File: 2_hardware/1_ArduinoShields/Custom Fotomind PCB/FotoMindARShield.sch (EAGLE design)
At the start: 11 parts

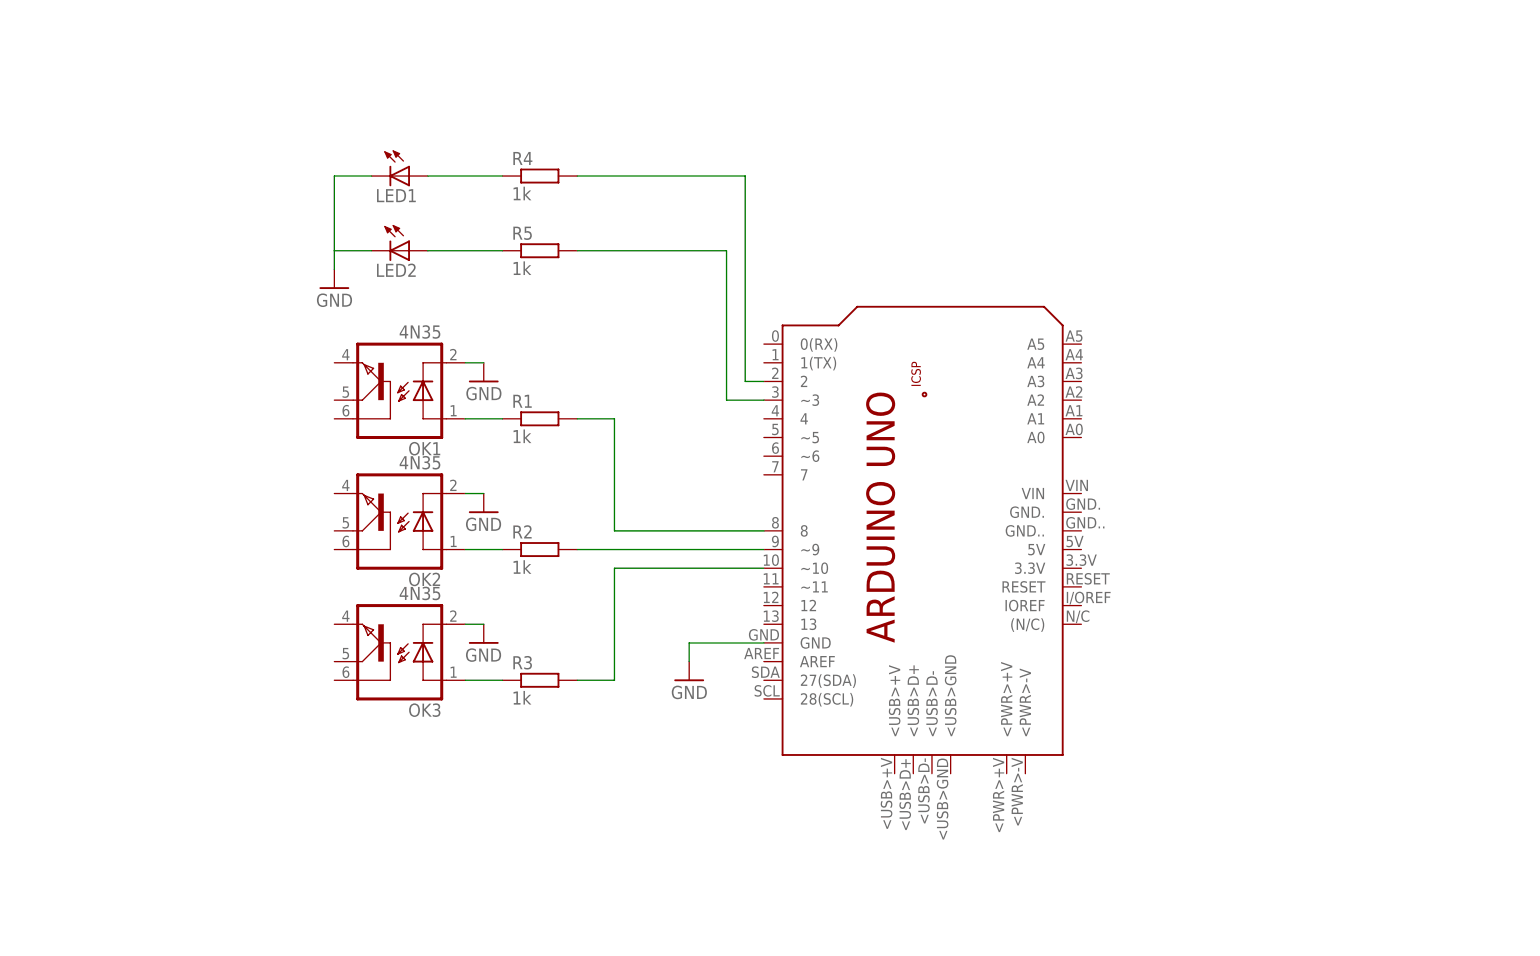
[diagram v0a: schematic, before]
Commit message: PCB: Added FotoResistor & Testbuttons
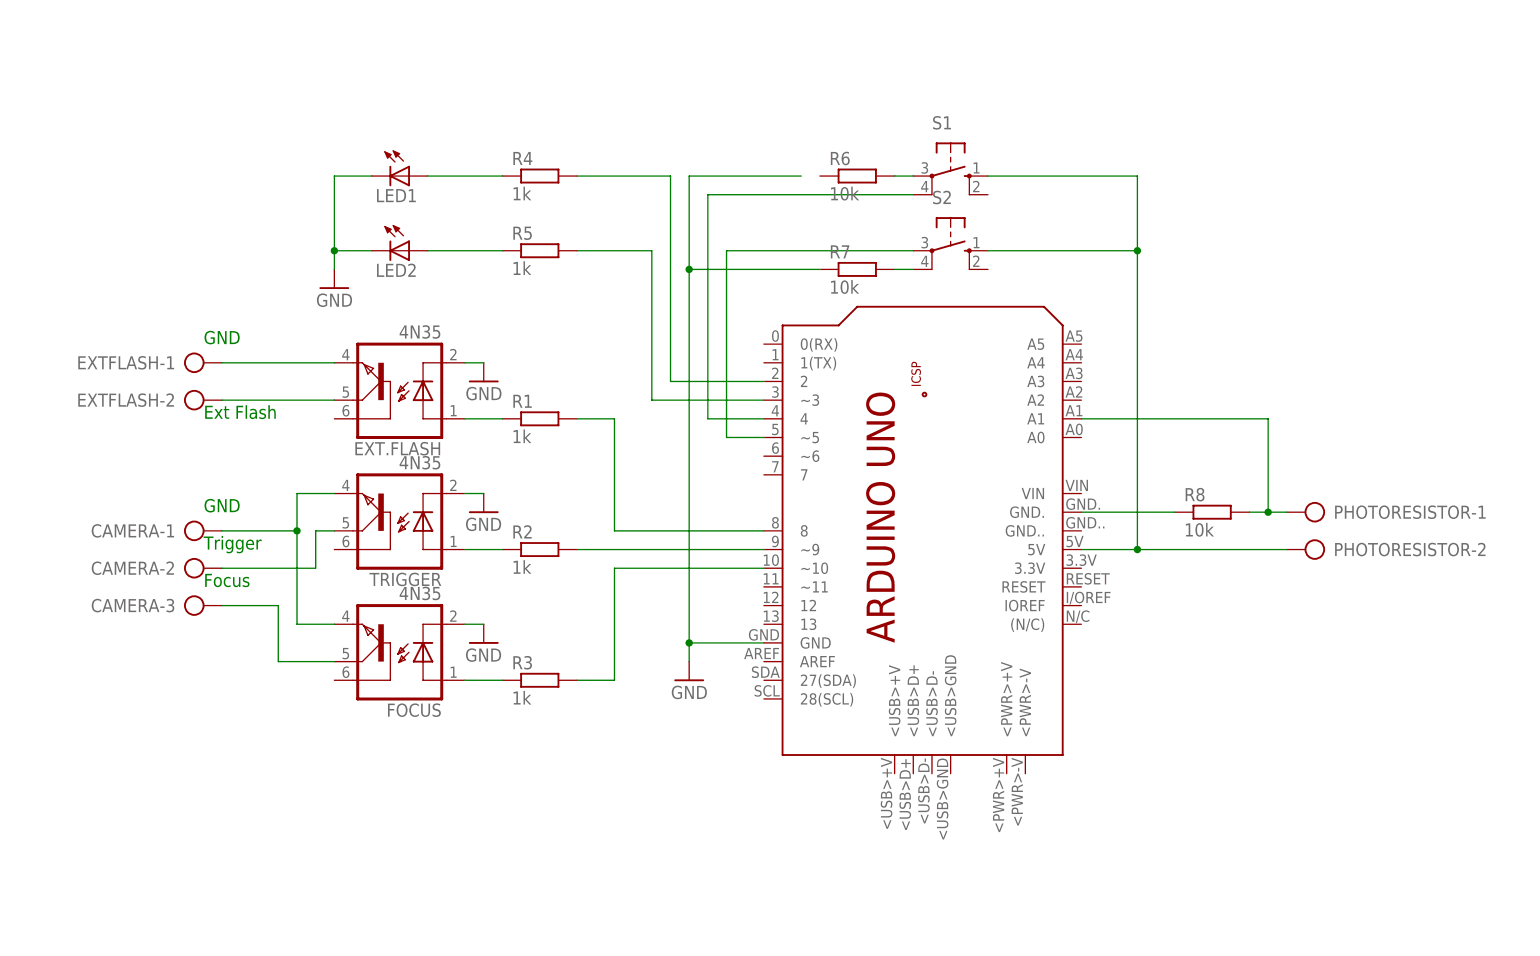
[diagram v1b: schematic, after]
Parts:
- added CAMERA: (no value), con-ptr500:AK300/3
- added EXTFLASH, PHOTORESISTOR: (no value), con-ptr500:AK300/2
- added R6, R7, R8: 10k, eagle-ltspice:R0204/7
- added S1, S2: (no value), switch-omron:10-XX
- renumbered OK1 to EXT.FLASH, OK2 to TRIGGER, OK3 to FOCUS
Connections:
- new net N$11: EXT.FLASH.EMI, EXTFLASH-1.KL
- new net N$12: EXT.FLASH.COL, EXTFLASH-2.KL
- new net N$13: CAMERA-1.KL, FOCUS.EMI, TRIGGER.EMI
- new net N$14: CAMERA-2.KL, TRIGGER.COL
- new net N$15: CAMERA-3.KL, FOCUS.COL
- new net N$16: PCB1.4, S1.P1
- new net N$17: PCB1.~5, S2.P
- new net N$18: R6.2, S1.P
- new net N$19: PCB1.5V, PHOTORESISTOR-2.KL, S1.S, S2.S
- new net N$20: R7.2, S2.P1
- new net N$21: PCB1.GND., R8.1
- new net N$22: PCB1.A1, PHOTORESISTOR-1.KL, R8.2
- net GND: now also R7.1
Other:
- note added: "Ext Flash"
- note added: "Focus"
- note added: "GND"
- note added: "Trigger"

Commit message: Added header for wireless-nRF24-communication
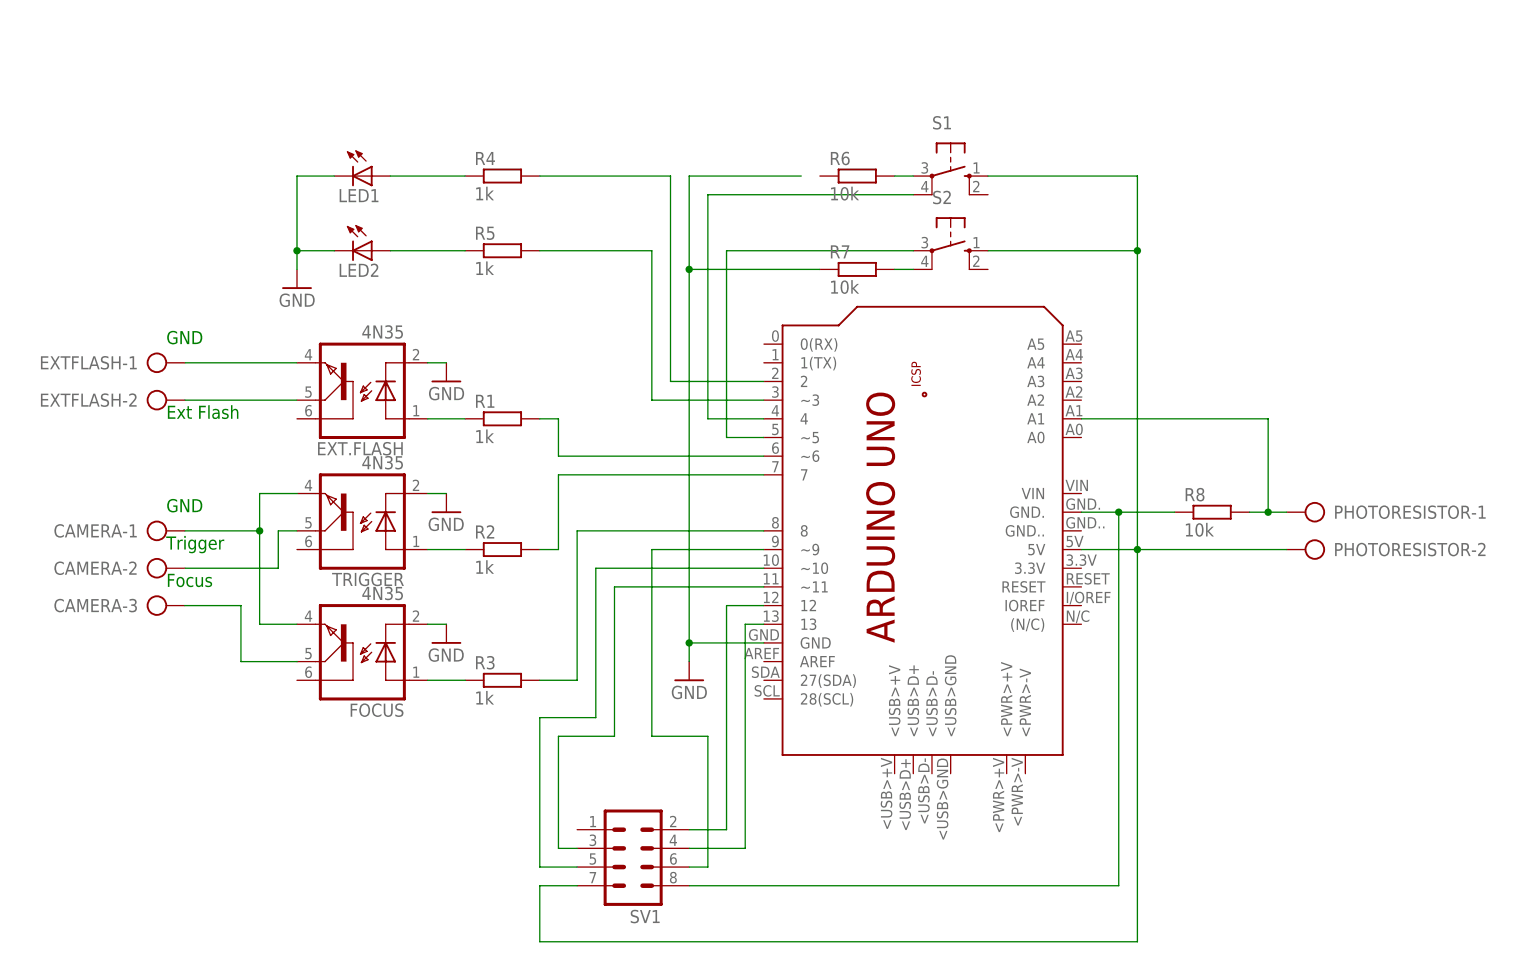
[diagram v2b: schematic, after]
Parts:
- added SV1: (no value), con-lstb:MA04-2
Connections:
- new net N$23: PCB1.12, SV1.2
- new net N$24: PCB1.~11, SV1.3
- new net N$25: PCB1.13, SV1.4
- new net N$26: PCB1.~10, SV1.5
- new net N$27: PCB1.~9, SV1.6
- net N$19: now also SV1.7
- net N$21: now also SV1.8
- net N$4: now also PCB1.~6; no longer PCB1.8
- net N$5: now also PCB1.7; no longer PCB1.~9
- net N$6: now also PCB1.8; no longer PCB1.~10
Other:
- moved on the sheet: CAMERA-1, CAMERA-2, CAMERA-3, EXT.FLASH, EXTFLASH-1, EXTFLASH-2, FOCUS, LED1, LED2, R1, R2, R3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

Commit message: Added Requirements + PCB progress
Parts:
- added EXTPOWER, EXTSENSOR: (no value), con-ptr500:AK300/2
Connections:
- new net N$28: EXTSENSOR-1.KL, PCB1.A0
- new net N$29: EXTSENSOR-2.KL, PCB1.A2
- new net N$30: PCB1.3.3V, SV1.7
- net GND: now also R6.1
- net N$19: now also EXTPOWER-2.KL; no longer SV1.7
- net N$21: now also EXTPOWER-1.KL
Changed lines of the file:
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@@
 <part name="R8" library="eagle-ltspice" deviceset="R" device="0204/7" value="10k"/>
 <part name="SV1" library="con-lstb" deviceset="MA04-2" device=""/>
+<part name="EXTPOWER" library="con-ptr500" deviceset="AK300/2" device="">
+<attribute name="MF" value=""/>
+<attribute name="MPN" value=""/>
+<attribute name="OC_FARNELL" value="unknown"/>
+<attribute name="OC_NEWARK" value="unknown"/>
+</part>
+<part name="EXTSENSOR" library="con-ptr500" deviceset="AK300/2" device="">
+<attribute name="MF" value=""/>
+<attribute name="MPN" value=""/>
+<attribute name="OC_FARNELL" value="unknown"/>
+<attribute name="OC_NEWARK" value="unknown"/>
+</part>
 </parts>
 <sheets>
@@
 <instance part="R8" gate="G$1" x="129.54" y="50.8"/>
 <instance part="SV1" gate="G$1" x="50.8" y="2.54" rot="R180"/>
+<instance part="EXTPOWER" gate="-1" x="144.78" y="66.04" rot="R180"/>
+<instance part="EXTPOWER" gate="-2" x="144.78" y="71.12" rot="R180"/>
+<instance part="EXTSENSOR" gate="-1" x="144.78" y="78.74" rot="R180"/>
+<instance part="EXTSENSOR" gate="-2" x="144.78" y="83.82" rot="R180"/>
 </instances>
 <busses>
@@
 <wire x1="68.58" y1="33.02" x2="58.42" y2="33.02" width="0.1524" layer="91"/>
 <wire x1="58.42" y1="33.02" x2="58.42" y2="30.48" width="0.1524" layer="91"/>
-<wire x1="73.66" y1="96.52" x2="58.42" y2="96.52" width="0.1524" layer="91"/>
+<wire x1="76.2" y1="96.52" x2="58.42" y2="96.52" width="0.1524" layer="91"/>
 <wire x1="58.42" y1="96.52" x2="58.42" y2="83.82" width="0.1524" layer="91"/>
 <junction x="58.42" y="33.02"/>
@@
 <wire x1="76.2" y1="83.82" x2="58.42" y2="83.82" width="0.1524" layer="91"/>
 <junction x="58.42" y="83.82"/>
+<pinref part="R6" gate="G$1" pin="1"/>
 </segment>
 </net>
@@
 <wire x1="119.38" y1="96.52" x2="119.38" y2="86.36" width="0.1524" layer="91"/>
 <pinref part="PCB1" gate="G$1" pin="5V"/>
-<wire x1="119.38" y1="86.36" x2="119.38" y2="45.72" width="0.1524" layer="91"/>
+<wire x1="119.38" y1="86.36" x2="119.38" y2="71.12" width="0.1524" layer="91"/>
+<wire x1="119.38" y1="71.12" x2="119.38" y2="45.72" width="0.1524" layer="91"/>
 <wire x1="119.38" y1="45.72" x2="111.76" y2="45.72" width="0.1524" layer="91"/>
 <pinref part="S2" gate="1" pin="S"/>
@@
 <wire x1="139.7" y1="45.72" x2="119.38" y2="45.72" width="0.1524" layer="91"/>
 <junction x="119.38" y="45.72"/>
-<wire x1="119.38" y1="45.72" x2="119.38" y2="-7.62" width="0.1524" layer="91"/>
-<wire x1="119.38" y1="-7.62" x2="38.1" y2="-7.62" width="0.1524" layer="91"/>
-<wire x1="38.1" y1="-7.62" x2="38.1" y2="0" width="0.1524" layer="91"/>
-<pinref part="SV1" gate="G$1" pin="7"/>
-<wire x1="38.1" y1="0" x2="43.18" y2="0" width="0.1524" layer="91"/>
+<pinref part="EXTPOWER" gate="-2" pin="KL"/>
+<wire x1="139.7" y1="71.12" x2="119.38" y2="71.12" width="0.1524" layer="91"/>
+<junction x="119.38" y="71.12"/>
 </segment>
 </net>
@@
 <wire x1="116.84" y1="0" x2="116.84" y2="50.8" width="0.1524" layer="91"/>
 <junction x="116.84" y="50.8"/>
+<pinref part="EXTPOWER" gate="-1" pin="KL"/>
+<wire x1="139.7" y1="66.04" x2="116.84" y2="66.04" width="0.1524" layer="91"/>
+<wire x1="116.84" y1="66.04" x2="116.84" y2="50.8" width="0.1524" layer="91"/>
 </segment>
 </net>
@@
 </segment>
 </net>
+<net name="N$28" class="0">
+<segment>
+<pinref part="EXTSENSOR" gate="-1" pin="KL"/>
+<wire x1="139.7" y1="78.74" x2="121.92" y2="78.74" width="0.1524" layer="91"/>
+<wire x1="121.92" y1="78.74" x2="121.92" y2="60.96" width="0.1524" layer="91"/>
+<pinref part="PCB1" gate="G$1" pin="A0"/>
+<wire x1="121.92" y1="60.96" x2="111.76" y2="60.96" width="0.1524" layer="91"/>
+</segment>
+</net>
+<net name="N$29" class="0">
+<segment>
+<pinref part="EXTSENSOR" gate="-2" pin="KL"/>
+<wire x1="139.7" y1="83.82" x2="114.3" y2="83.82" width="0.1524" layer="91"/>
+<wire x1="114.3" y1="83.82" x2="114.3" y2="66.04" width="0.1524" layer="91"/>
+<pinref part="PCB1" gate="G$1" pin="A2"/>
+<wire x1="114.3" y1="66.04" x2="111.76" y2="66.04" width="0.1524" layer="91"/>
+</segment>
+</net>
+<net name="N$30" class="0">
+<segment>
+<pinref part="SV1" gate="G$1" pin="7"/>
+<wire x1="43.18" y1="0" x2="38.1" y2="0" width="0.1524" layer="91"/>
+<wire x1="38.1" y1="0" x2="38.1" y2="-7.62" width="0.1524" layer="91"/>
+<wire x1="38.1" y1="-7.62" x2="119.38" y2="-7.62" width="0.1524" layer="91"/>
+<wire x1="119.38" y1="-7.62" x2="119.38" y2="43.18" width="0.1524" layer="91"/>
+<pinref part="PCB1" gate="G$1" pin="3.3V"/>
+<wire x1="119.38" y1="43.18" x2="111.76" y2="43.18" width="0.1524" layer="91"/>
+</segment>
+</net>

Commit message: New ultrasonic feature
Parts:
- added LED3: (no value), led:LED3MM
- added R9: 1k, eagle-ltspice:R0204/7
- added X1: ULTRASOON, con-molex:22-23-2041
- S1: value (none) -> Trigger
- S2: value (none) -> Flash
- SV1: value (none) -> Wireless nRF24
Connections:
- removed net N$19: EXTPOWER-2.KL, PCB1.5V, PHOTORESISTOR-2.KL, S1.S, S2.S
- new net N$105: PCB1.0(RX), X1-3.S
- new net N$107: PCB1.1(TX), X1-2.S
- new net N$79: EXTPOWER-2.KL, PCB1.5V, PHOTORESISTOR-2.KL, R9.2, S1.S, S2.S, X1-4.S
- new net N$92: LED1.A, R9.1
- net GND: now also LED3.C
- net N$10: now also LED2.A; no longer LED1.A
- net N$21: now also X1-1.S
- net N$9: now also LED3.A; no longer LED2.A
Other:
- moved on the sheet: LED1, LED2, R4, R5, R6, R7, S1, S2

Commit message: Final PCB-design, ready to mill ! (+groundplane)
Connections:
- removed net N$107: PCB1.1(TX), X1-2.S
- new net N$106: PCB1.0(RX), X1-2.S
- net N$105: now also PCB1.1(TX); no longer PCB1.0(RX)
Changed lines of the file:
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@@
 <net name="N$105" class="0">
 <segment>
-<wire x1="137.16" y1="86.36" x2="111.76" y2="86.36" width="0.1524" layer="91"/>
-<wire x1="111.76" y1="86.36" x2="111.76" y2="83.82" width="0.1524" layer="91"/>
-<wire x1="111.76" y1="83.82" x2="68.58" y2="83.82" width="0.1524" layer="91"/>
-<wire x1="68.58" y1="83.82" x2="68.58" y2="73.66" width="0.1524" layer="91"/>
-<pinref part="PCB1" gate="G$1" pin="0(RX)"/>
-<wire x1="137.16" y1="86.36" x2="137.16" y2="96.52" width="0.1524" layer="91"/>
+<pinref part="PCB1" gate="G$1" pin="1(TX)"/>
+<wire x1="66.04" y1="71.12" x2="68.58" y2="71.12" width="0.1524" layer="91"/>
 <pinref part="X1" gate="-3" pin="S"/>
-<wire x1="137.16" y1="96.52" x2="139.7" y2="96.52" width="0.1524" layer="91"/>
+<wire x1="139.7" y1="96.52" x2="124.46" y2="96.52" width="0.1524" layer="91"/>
+<wire x1="124.46" y1="96.52" x2="124.46" y2="88.9" width="0.1524" layer="91"/>
+<wire x1="124.46" y1="88.9" x2="109.22" y2="88.9" width="0.1524" layer="91"/>
+<wire x1="109.22" y1="88.9" x2="109.22" y2="83.82" width="0.1524" layer="91"/>
+<wire x1="109.22" y1="83.82" x2="66.04" y2="83.82" width="0.1524" layer="91"/>
+<wire x1="66.04" y1="83.82" x2="66.04" y2="71.12" width="0.1524" layer="91"/>
 </segment>
 </net>
-<net name="N$107" class="0">
+<net name="N$106" class="0">
 <segment>
 <pinref part="X1" gate="-2" pin="S"/>
-<wire x1="134.62" y1="99.06" x2="139.7" y2="99.06" width="0.1524" layer="91"/>
-<wire x1="134.62" y1="99.06" x2="134.62" y2="88.9" width="0.1524" layer="91"/>
-<wire x1="134.62" y1="88.9" x2="109.22" y2="88.9" width="0.1524" layer="91"/>
-<wire x1="109.22" y1="88.9" x2="109.22" y2="86.36" width="0.1524" layer="91"/>
-<wire x1="109.22" y1="86.36" x2="66.04" y2="86.36" width="0.1524" layer="91"/>
-<wire x1="66.04" y1="86.36" x2="66.04" y2="71.12" width="0.1524" layer="91"/>
-<pinref part="PCB1" gate="G$1" pin="1(TX)"/>
-<wire x1="66.04" y1="71.12" x2="68.58" y2="71.12" width="0.1524" layer="91"/>
+<wire x1="139.7" y1="99.06" x2="121.92" y2="99.06" width="0.1524" layer="91"/>
+<wire x1="121.92" y1="99.06" x2="121.92" y2="86.36" width="0.1524" layer="91"/>
+<wire x1="121.92" y1="86.36" x2="111.76" y2="86.36" width="0.1524" layer="91"/>
+<wire x1="111.76" y1="86.36" x2="111.76" y2="81.28" width="0.1524" layer="91"/>
+<pinref part="PCB1" gate="G$1" pin="0(RX)"/>
+<wire x1="111.76" y1="81.28" x2="68.58" y2="81.28" width="0.1524" layer="91"/>
+<wire x1="68.58" y1="81.28" x2="68.58" y2="73.66" width="0.1524" layer="91"/>
 </segment>
 </net>
